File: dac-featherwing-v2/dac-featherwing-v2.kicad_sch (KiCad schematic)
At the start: 11 parts, among them J1 BOT, J2 TOP, J3 35RASMT4BHNTRX, U1 WM1824CGEFL, U2 TLV320AIC3104IRHBR

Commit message: Dac featherwing schematic v2
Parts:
- removed C1, C2, C5: 4.7uF, Capacitor_SMD:C_0805_2012Metric_Pad1.15x1.40mm_HandSolder, symbol Device:C_Small
- removed C3, C4: 1uF, Capacitor_SMD:C_0805_2012Metric_Pad1.15x1.40mm_HandSolder, symbol Device:C_Small
- removed C6: 2.2uF, Capacitor_SMD:C_0805_2012Metric_Pad1.15x1.40mm_HandSolder, symbol Device:C_Small
- removed J3: 35RASMT4BHNTRX, SWITCHCRAFT_35RASMT4BHNTRX, symbol 35RASMT4BHNTRX:35RASMT4BHNTRX
- removed U1: WM1824CGEFL, Package_DFN_QFN:QFN-24-1EP_4x4mm_P0.5mm_EP2.6x2.6mm, symbol WM1824CGEFL:WM1824CGEFL
- removed U2: TLV320AIC3104IRHBR, Footprints:IC_ADS125H01IRHBT, symbol TLV320AIC3104IRHBR:TLV320AIC3104IRHBR
- added C?: 10uF, symbol Device:C_Polarized
- added C? (x4): 10uF, symbol Device:C_Polarized_Small
- added C? (x4): 0.1uF, symbol Device:C_Small
- added C? (x2): 220uF, symbol Device:C_Polarized
- added C? (x2): 1uF, symbol Device:C_Polarized
- added C?: 0.1uF, symbol Device:C
- added J? (x2): AudioJack4, symbol Connector:AudioJack4
- added R? (x3): 100, symbol Device:R_Small
- added R? (x2): 4.7K, symbol Device:R_Small
- added R? (x4): 47K, symbol Device:R_Small
- added R?: 10K, symbol Device:R_Small
- added U?: WM8731CLSEFL, Package_DFN_QFN:QFN-28-1EP_5x5mm_P0.5mm_EP3.35x3.35mm, symbol Audio:WM8731CLSEFL
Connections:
- net +3.3VA: now also C?.1, C?.1, C?.1, C?.1, U?.12 (HPVDD), U?.18 (AVDD)
- net +3V3: now also C?.1, C?.1, C?.1, C?.1, R?.1, R?.2, U?.3 (DCVDD), U?.5 (DBVDD)
- net GND: now also C?.2, C?.2, C?.2, C?.2, C?.2, C?.2, C?.2, C?.2, C?.2, C?.2, J?.S, J?.S, R?.1, R?.1, R?.2, R?.2, R?.2, U?.15 (HPGND), U?.19 (AGND), U?.26 (~CSB), U?.29 (AGND), U?.4 (DGND)
- net I2S_BCK: now also U?.7 (BCLK)
- net I2S_DO: now also U?.8 (DACDAT)
- net I2S_WS: now also U?.9 (DACLRC)
- net SCL: now also R?.1, U?.28 (SCLK)
- net SDA: now also R?.2, U?.27 (SDIN)
- net U1RXD/CLK_OUT3 renamed I2S_MCLK
- net I2S_MCLK: now also U?.1 (XTI/MCLK)
- new net: R?.2, U?.6 (CLKOUT)
- new net: C?.1, C?.1, U?.20 (VMID)
- new net: C?.2, R?.1, R?.2
- new net: C?.1, U?.13 (LHPOUT)
- new net: C?.1, U?.16 (LOUT)
- new net: C?.1, U?.14 (RHPOUT)
- new net: C?.1, U?.17 (ROUT)
- new net: R?.1, U?.25 (MODE)
- new net: C?.2, R?.1, R?.1
- new net CLKOUT: R?.1
- new net LHPOUT: C?.2, J?.T, R?.2
- new net LOUT: J?.T, R?.2
- new net RHPOUT: C?.2, J?.R1, R?.1
- new net ROUT: J?.R1, R?.2
- no-connect marks 0 -> 7
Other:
- note added: "TODO CHECK 3V3A OUTPUT ON REAL FEATHER"
- moved on the sheet: J1, J2

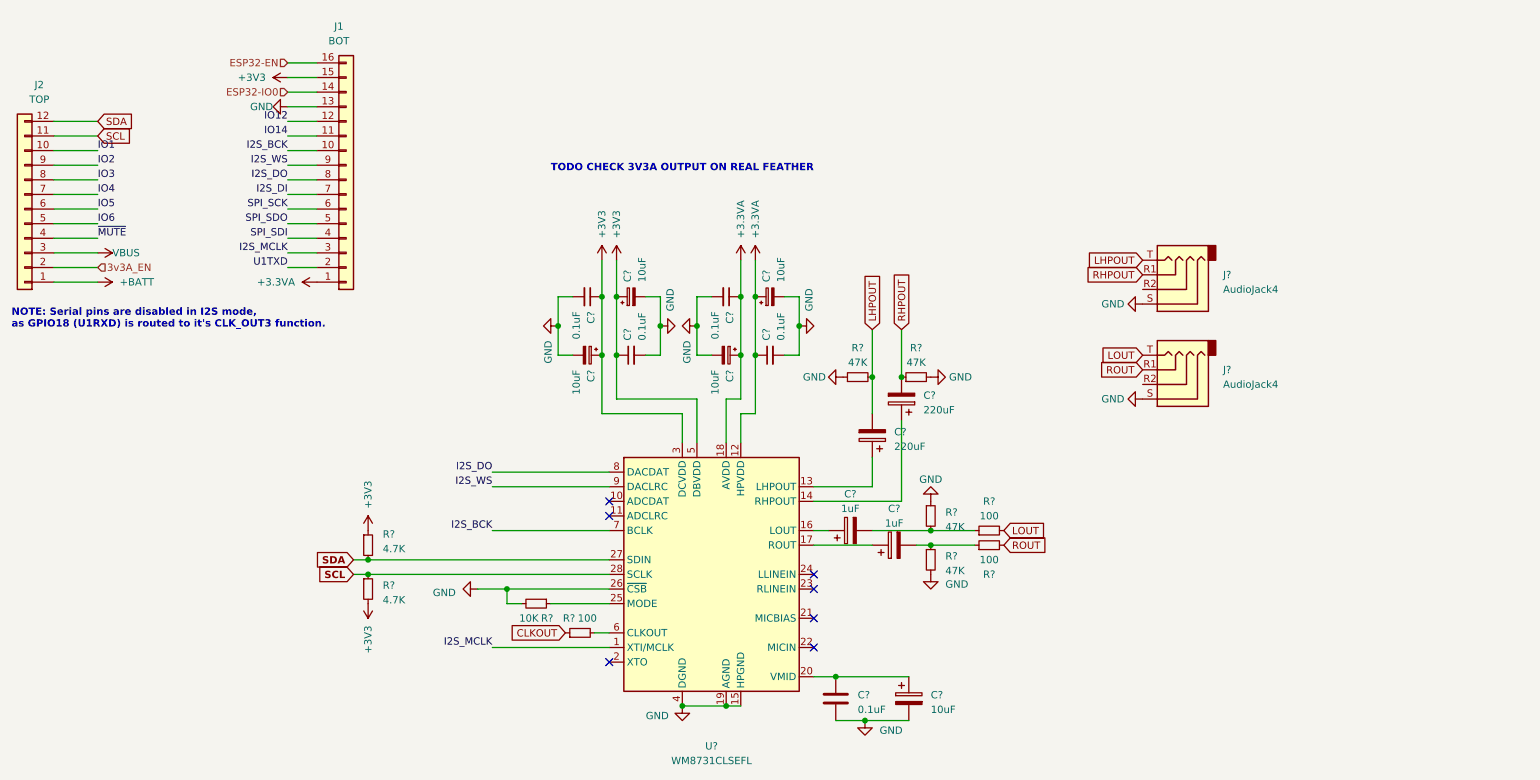
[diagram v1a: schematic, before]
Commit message: Work on DAC Featherwing v2
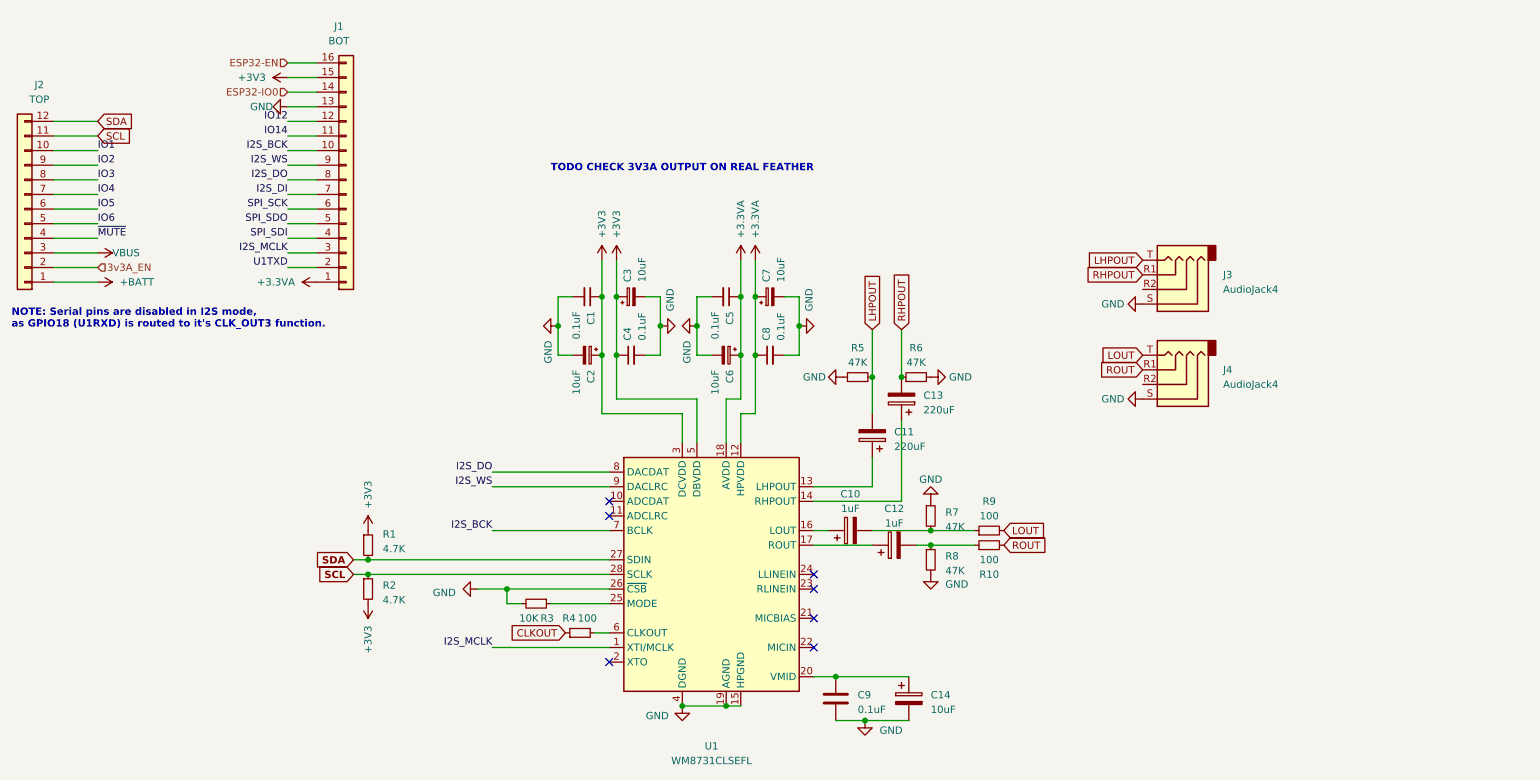
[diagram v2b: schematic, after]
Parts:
- C1, C4, C5, C8, C9: renamed from C?; footprint (none) -> Capacitor_SMD:C_0805_2012Metric_Pad1.18x1.45mm_HandSolder
- C10, C12: renamed from C?; footprint (none) -> Capacitor_SMD:CP_Elec_4x4.5
- C11, C13: renamed from C?; footprint (none) -> Capacitor_SMD:CP_Elec_8x10
- C14, C2, C3, C6, C7: renamed from C?; footprint (none) -> Capacitor_Tantalum_SMD:CP_EIA-6032-20_AVX-F_Pad2.25x2.35mm_HandSolder
- J3, J4: renamed from J?; footprint (none) -> Connector_Audio:Jack_3.5mm_PJ311_Horizontal
- R1, R10, R2, R3, R4, R5, R6, R7, R8, R9: renamed from R?; footprint (none) -> Resistor_SMD:R_0805_2012Metric_Pad1.20x1.40mm_HandSolder
- gave numbers to parts that had none: 1

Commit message: Capacitors checked. TRRS pins checked. 3.5mm Footprint made. Performing layout and routing.
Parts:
- removed R4: 100, Resistor_SMD:R_0805_2012Metric_Pad1.20x1.40mm_HandSolder, symbol Device:R_Small
- C2, C3: footprint Capacitor_Tantalum_SMD:CP_EIA-6032-20_AVX-F_Pad2.25x2.35mm_HandSolder -> Capacitor_SMD:C_0805_2012Metric_Pad1.18x1.45mm_HandSolder
- J3, J4: footprint Connector_Audio:Jack_3.5mm_PJ311_Horizontal -> Footprints:Lumberg 1503 20 VP3
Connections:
- net GND: now also J3.R2, J4.R2
- net LHPOUT: now also C13.2, R6.1; no longer C11.2, R5.2
- net RHPOUT: now also C11.2, R5.2; no longer C13.2, R6.1
- net at C11.1: now also U1.14 (RHPOUT); no longer U1.13 (LHPOUT)
- net at C13.1: now also U1.13 (LHPOUT); no longer U1.14 (RHPOUT)
- no-connect marks 7 -> 8
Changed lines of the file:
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@@
   (no_connect (at 121.92 99.06))
   (no_connect (at 121.92 101.6))
+  (no_connect (at 121.92 121.92))
   (no_connect (at 121.92 127))
   (no_connect (at 157.48 111.76))
@@
     (stroke (width 0) (type solid) (color 0 0 0 0))
   )
-  (wire (pts (xy 119.38 121.92) (xy 121.92 121.92))
-    (stroke (width 0) (type solid) (color 0 0 0 0))
-  )
   (wire (pts (xy 120.65 57.15) (xy 120.65 63.5))
     (stroke (width 0) (type solid) (color 0 0 0 0))
@@
     (stroke (width 0) (type solid) (color 0 0 0 0))
   )
-  (wire (pts (xy 157.48 96.52) (xy 167.64 96.52))
-    (stroke (width 0) (type solid) (color 0 0 0 0))
-  )
-  (wire (pts (xy 157.48 99.06) (xy 172.72 99.06))
+  (wire (pts (xy 157.48 96.52) (xy 172.72 96.52))
+    (stroke (width 0) (type solid) (color 0 0 0 0))
+  )
+  (wire (pts (xy 157.48 99.06) (xy 167.64 99.06))
     (stroke (width 0) (type solid) (color 0 0 0 0))
   )
@@
     (stroke (width 0) (type solid) (color 0 0 0 0))
   )
-  (wire (pts (xy 167.64 96.52) (xy 167.64 91.44))
+  (wire (pts (xy 167.64 91.44) (xy 167.64 99.06))
     (stroke (width 0) (type solid) (color 0 0 0 0))
   )
@@
     (stroke (width 0) (type solid) (color 0 0 0 0))
   )
-  (wire (pts (xy 172.72 99.06) (xy 172.72 85.09))
+  (wire (pts (xy 172.72 96.52) (xy 172.72 85.09))
     (stroke (width 0) (type solid) (color 0 0 0 0))
   )
@@
     )
   )
-  (global_label "CLKOUT" (shape input) (at 114.3 121.92 180) (fields_autoplaced)
-    (effects (font (size 1.27 1.27)) (justify right))
-    (property "Intersheet References" "${INTERSHEET_REFS}" (id 0) (at 104.6902 121.8406 0)
-      (effects (font (size 1.27 1.27)) (justify right) hide)
-    )
-  )
-  (global_label "LHPOUT" (shape input) (at 167.64 69.215 90) (fields_autoplaced)
+  (global_label "RHPOUT" (shape input) (at 167.64 69.215 90) (fields_autoplaced)
     (effects (font (size 1.27 1.27)) (justify left))
-    (property "Intersheet References" "${INTERSHEET_REFS}" (id 0) (at 167.5606 59.5448 90)
+    (property "Intersheet References" "${INTERSHEET_REFS}" (id 0) (at 167.5606 59.3029 90)
       (effects (font (size 1.27 1.27)) (justify left) hide)
     )
   )
-  (global_label "RHPOUT" (shape input) (at 172.72 69.215 90) (fields_autoplaced)
+  (global_label "LHPOUT" (shape input) (at 172.72 69.215 90) (fields_autoplaced)
     (effects (font (size 1.27 1.27)) (justify left))
-    (property "Intersheet References" "${INTERSHEET_REFS}" (id 0) (at 172.6406 59.3029 90)
+    (property "Intersheet References" "${INTERSHEET_REFS}" (id 0) (at 172.6406 59.5448 90)
       (effects (font (size 1.27 1.27)) (justify left) hide)
     )
@@
     (pin "1")
   )
+  (symbol (lib_id "power:GND") (at 214.63 62.23 270) (unit 1)
+    (in_bom yes) (on_board yes)
+    (property "Reference" "#PWR0125" (id 0) (at 208.28 62.23 0)
+      (effects (font (size 1.27 1.27)) hide)
+    )
+    (property "Value" "GND" (id 1) (at 211.455 62.2301 90)
+      (effects (font (size 1.27 1.27)) (justify right))
+    )
+    (property "Footprint" "" (id 2) (at 214.63 62.23 0)
+      (effects (font (size 1.27 1.27)) hide)
+    )
+    (property "Datasheet" "" (id 3) (at 214.63 62.23 0)
+      (effects (font (size 1.27 1.27)) hide)
+    )
+    (pin "1")
+  )
   (symbol (lib_id "power:GND") (at 214.63 64.77 270) (unit 1)
     (in_bom yes) (on_board yes)
@@
     )
     (property "Datasheet" "" (id 3) (at 214.63 64.77 0)
+      (effects (font (size 1.27 1.27)) hide)
+    )
+    (pin "1")
+  )
+  (symbol (lib_id "power:GND") (at 214.63 78.74 270) (unit 1)
+    (in_bom yes) (on_board yes)
+    (property "Reference" "#PWR0126" (id 0) (at 208.28 78.74 0)
+      (effects (font (size 1.27 1.27)) hide)
+    )
+    (property "Value" "GND" (id 1) (at 211.455 78.7401 90)
+      (effects (font (size 1.27 1.27)) (justify right))
+    )
+    (property "Footprint" "" (id 2) (at 214.63 78.74 0)
+      (effects (font (size 1.27 1.27)) hide)
+    )
+    (property "Datasheet" "" (id 3) (at 214.63 78.74 0)
       (effects (font (size 1.27 1.27)) hide)
     )
@@
     (pin "2")
   )
-  (symbol (lib_id "Device:R_Small") (at 116.84 121.92 90) (unit 1)
-    (in_bom yes) (on_board yes)
-    (property "Reference" "R4" (id 0) (at 114.935 119.38 90))
-    (property "Value" "100" (id 1) (at 118.11 119.38 90))
-    (property "Footprint" "Resistor_SMD:R_0805_2012Metric_Pad1.20x1.40mm_HandSolder" (id 2) (at 116.84 121.92 0)
-      (effects (font (size 1.27 1.27)) hide)
-    )
-    (property "Datasheet" "~" (id 3) (at 116.84 121.92 0)
-      (effects (font (size 1.27 1.27)) hide)
-    )
-    (pin "1")
-    (pin "2")
-  )
   (symbol (lib_id "Device:R_Small") (at 165.1 77.47 90) (unit 1)
     (in_bom yes) (on_board yes) (fields_autoplaced)
@@
       (effects (font (size 1.27 1.27)) (justify left))
     )
-    (property "Footprint" "Capacitor_Tantalum_SMD:CP_EIA-6032-20_AVX-F_Pad2.25x2.35mm_HandSolder" (id 2) (at 118.11 73.66 0)
+    (property "Footprint" "Capacitor_SMD:C_0805_2012Metric_Pad1.18x1.45mm_HandSolder" (id 2) (at 118.11 73.66 0)
       (effects (font (size 1.27 1.27)) hide)
     )
@@
       (effects (font (size 1.27 1.27)) (justify left))
     )
-    (property "Footprint" "Capacitor_Tantalum_SMD:CP_EIA-6032-20_AVX-F_Pad2.25x2.35mm_HandSolder" (id 2) (at 125.73 63.5 0)
+    (property "Footprint" "Capacitor_SMD:C_0805_2012Metric_Pad1.18x1.45mm_HandSolder" (id 2) (at 125.73 63.5 0)
       (effects (font (size 1.27 1.27)) hide)
     )
@@
       (effects (font (size 1.27 1.27)) (justify right))
     )
-    (property "Footprint" "Connector_Audio:Jack_3.5mm_PJ311_Horizontal" (id 2) (at 219.71 62.23 0)
+    (property "Footprint" "Footprints:Lumberg 1503 20 VP3" (id 2) (at 219.71 62.23 0)
       (effects (font (size 1.27 1.27)) hide)
     )
@@
       (effects (font (size 1.27 1.27)) (justify right))
     )
-    (property "Footprint" "Connector_Audio:Jack_3.5mm_PJ311_Horizontal" (id 2) (at 219.71 78.74 0)
+    (property "Footprint" "Footprints:Lumberg 1503 20 VP3" (id 2) (at 219.71 78.74 0)
       (effects (font (size 1.27 1.27)) hide)
     )
@@
       (reference "#PWR0124") (unit 1) (value "GND") (footprint "")
     )
+    (path "/2b651d2a-e56e-4d48-bd9b-b60896a6b09c"
+      (reference "#PWR0125") (unit 1) (value "GND") (footprint "")
+    )
+    (path "/fa5b50aa-4a40-461a-8ba0-ab84f8336699"
+      (reference "#PWR0126") (unit 1) (value "GND") (footprint "")
+    )
     (path "/1ca37de6-2e96-420b-a373-4aae964d1d81"
       (reference "C1") (unit 1) (value "0.1uF") (footprint "Capacitor_SMD:C_0805_2012Metric_Pad1.18x1.45mm_HandSolder")
     )
     (path "/b8d44a4d-4ce5-4f63-83bc-ac18e2274e55"
-      (reference "C2") (unit 1) (value "10uF") (footprint "Capacitor_Tantalum_SMD:CP_EIA-6032-20_AVX-F_Pad2.25x2.35mm_HandSolder")
+      (reference "C2") (unit 1) (value "10uF") (footprint "Capacitor_SMD:C_0805_2012Metric_Pad1.18x1.45mm_HandSolder")
     )
     (path "/5266d3fa-3451-4251-bc88-9b13cd0dbac5"
-      (reference "C3") (unit 1) (value "10uF") (footprint "Capacitor_Tantalum_SMD:CP_EIA-6032-20_AVX-F_Pad2.25x2.35mm_HandSolder")
+      (reference "C3") (unit 1) (value "10uF") (footprint "Capacitor_SMD:C_0805_2012Metric_Pad1.18x1.45mm_HandSolder")
     )
     (path "/6033a536-78dd-44a3-afcb-e66f9f9a9fbb"
@@
     )
     (path "/20e7942a-6128-4485-b28c-2f17c65e05fe"
-      (reference "J3") (unit 1) (value "AudioJack4") (footprint "Connector_Audio:Jack_3.5mm_PJ311_Horizontal")
+      (reference "J3") (unit 1) (value "AudioJack4") (footprint "Footprints:Lumberg 1503 20 VP3")
     )
     (path "/8994dec6-bc06-4528-ac34-a1696a8c8670"
-      (reference "J4") (unit 1) (value "AudioJack4") (footprint "Connector_Audio:Jack_3.5mm_PJ311_Horizontal")
+      (reference "J4") (unit 1) (value "AudioJack4") (footprint "Footprints:Lumberg 1503 20 VP3")
     )
     (path "/1abb9351-ad36-4fb2-b13b-3ae130f82d03"
@@
       (reference "R3") (unit 1) (value "10K") (footprint "Resistor_SMD:R_0805_2012Metric_Pad1.20x1.40mm_HandSolder")
     )
-    (path "/0d249cd2-d195-465b-a18e-a33385de8911"
-      (reference "R4") (unit 1) (value "100") (footprint "Resistor_SMD:R_0805_2012Metric_Pad1.20x1.40mm_HandSolder")
-    )
     (path "/6722b7f9-bdf8-4b01-bd5a-b89d60aff490"

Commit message: Full route #1 complete
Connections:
- net LOUT: now also R10.2; no longer R9.2
- net ROUT: now also R9.2; no longer R10.2
- net at C10.1: now also U1.17 (ROUT); no longer U1.16 (LOUT)
- net at C12.1: now also U1.16 (LOUT); no longer U1.17 (ROUT)
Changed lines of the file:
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@@
     (stroke (width 0) (type solid) (color 0 0 0 0))
   )
-  (wire (pts (xy 157.48 104.14) (xy 160.02 104.14))
-    (stroke (width 0) (type solid) (color 0 0 0 0))
-  )
-  (wire (pts (xy 157.48 106.68) (xy 167.64 106.68))
+  (wire (pts (xy 157.48 104.14) (xy 159.385 104.14))
     (stroke (width 0) (type solid) (color 0 0 0 0))
   )
   (wire (pts (xy 157.48 129.54) (xy 161.29 129.54))
+    (stroke (width 0) (type solid) (color 0 0 0 0))
+  )
+  (wire (pts (xy 159.385 104.14) (xy 159.385 105.41))
+    (stroke (width 0) (type solid) (color 0 0 0 0))
+  )
+  (wire (pts (xy 159.385 105.41) (xy 160.655 105.41))
+    (stroke (width 0) (type solid) (color 0 0 0 0))
+  )
+  (wire (pts (xy 160.02 104.14) (xy 160.02 106.68))
+    (stroke (width 0) (type solid) (color 0 0 0 0))
+  )
+  (wire (pts (xy 160.02 106.68) (xy 157.48 106.68))
+    (stroke (width 0) (type solid) (color 0 0 0 0))
+  )
+  (wire (pts (xy 160.655 105.41) (xy 160.655 106.68))
+    (stroke (width 0) (type solid) (color 0 0 0 0))
+  )
+  (wire (pts (xy 160.655 106.68) (xy 167.64 106.68))
     (stroke (width 0) (type solid) (color 0 0 0 0))
   )
@@
     )
   )
-  (global_label "LOUT" (shape input) (at 190.5 104.14 0) (fields_autoplaced)
+  (global_label "ROUT" (shape input) (at 190.5 104.14 0) (fields_autoplaced)
     (effects (font (size 1.27 1.27)) (justify left))
-    (property "Intersheet References" "${INTERSHEET_REFS}" (id 0) (at 197.5698 104.0606 0)
+    (property "Intersheet References" "${INTERSHEET_REFS}" (id 0) (at 197.8117 104.0606 0)
       (effects (font (size 1.27 1.27)) (justify left) hide)
     )
   )
-  (global_label "ROUT" (shape input) (at 190.5 106.68 0) (fields_autoplaced)
+  (global_label "LOUT" (shape input) (at 190.5 106.68 0) (fields_autoplaced)
     (effects (font (size 1.27 1.27)) (justify left))
-    (property "Intersheet References" "${INTERSHEET_REFS}" (id 0) (at 197.8117 106.6006 0)
+    (property "Intersheet References" "${INTERSHEET_REFS}" (id 0) (at 197.5698 106.6006 0)
       (effects (font (size 1.27 1.27)) (justify left) hide)
     )
